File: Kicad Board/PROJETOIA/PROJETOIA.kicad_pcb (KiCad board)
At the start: 2 copper layers, 2 parts

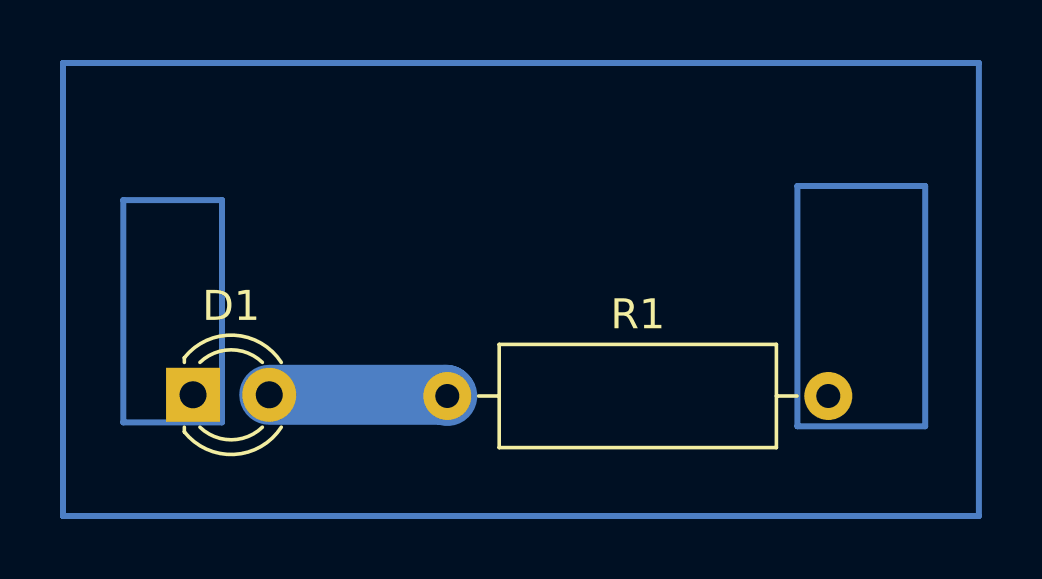
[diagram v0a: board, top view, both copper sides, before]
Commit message: Upload Rotas to GCODE
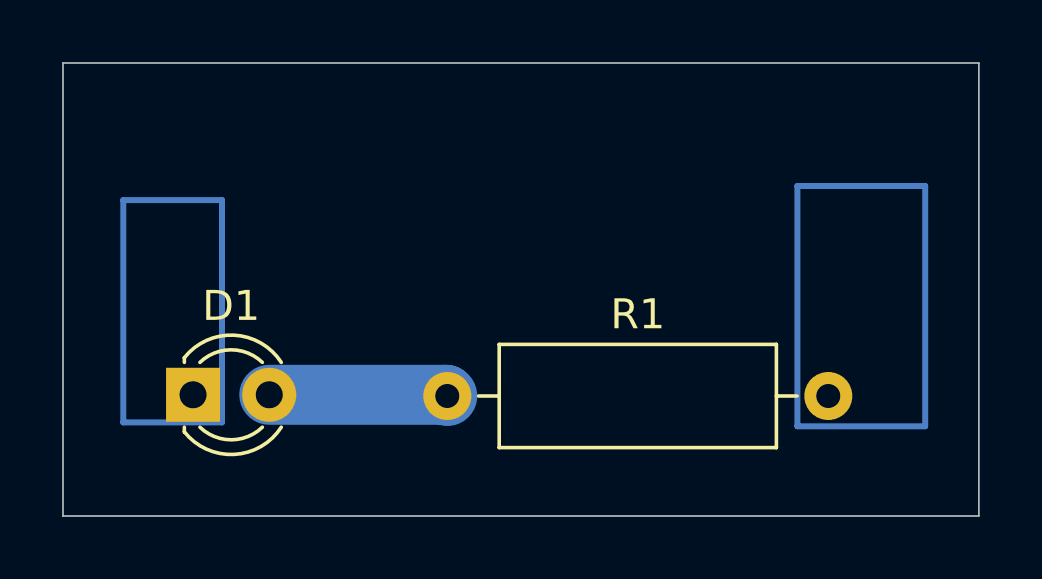
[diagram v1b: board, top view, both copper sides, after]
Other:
- board outline added: 30.5 x 15.1 mm
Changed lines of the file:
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@@
 		(allow_soldermask_bridges_in_footprints no)
 		(pcbplotparams
-			(layerselection 0x00010fc_ffffffff)
-			(plot_on_all_layers_selection 0x0000000_00000000)
+			(layerselection 0x0001000_7ffffffe)
+			(plot_on_all_layers_selection 0x0001000_00000000)
 			(disableapertmacros no)
 			(usegerberextensions no)
@@
 			(outputformat 1)
 			(mirror no)
-			(drillshape 1)
+			(drillshape 0)
 			(scaleselection 1)
-			(outputdirectory "")
+			(outputdirectory "CNC/")
 		)
 	)
@@
 	)
 	(gr_rect
-		(start 58.47 51.07)
-		(end 89 66.17)
-		(stroke
-			(width 0.2)
-			(type default)
-		)
-		(fill none)
-		(layer "B.Cu")
-	)
-	(gr_rect
 		(start 82.95 55.17)
 		(end 87.21 63.18)
@@
 		(layer "B.Cu")
 		(net 2)
+	)
+	(gr_rect
+		(start 58.47 51.07)
+		(end 89 66.17)
+		(stroke
+			(width 0.05)
+			(type default)
+		)
+		(fill none)
+		(layer "Edge.Cuts")
 	)
 	(segment
@@
 		(min_thickness 0.25)
 		(filled_areas_thickness no)
-		(fill
+		(fill yes
 			(thermal_gap 0.5)
 			(thermal_bridge_width 0.5)
@@
 		(min_thickness 0.25)
 		(filled_areas_thickness no)
-		(fill
+		(fill yes
 			(thermal_gap 0.5)
 			(thermal_bridge_width 0.5)
